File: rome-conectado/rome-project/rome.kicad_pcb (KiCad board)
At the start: 2 copper layers, 109.2 x 86.4 mm, 24 parts, among them J1 Screw_Terminal_01x02, J2 Conn_02x04_Counter_Clockwise, U3 L7805

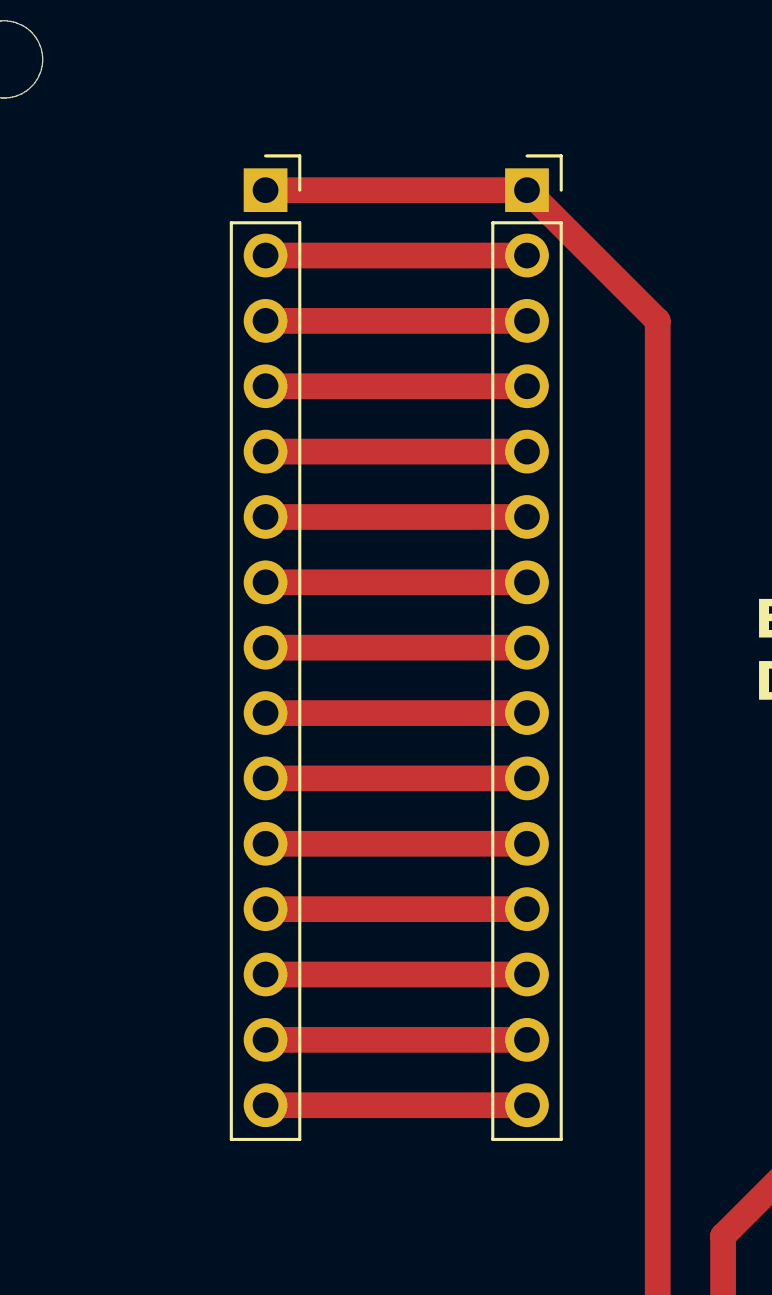
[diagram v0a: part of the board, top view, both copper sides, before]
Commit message: Update board after position adjustments
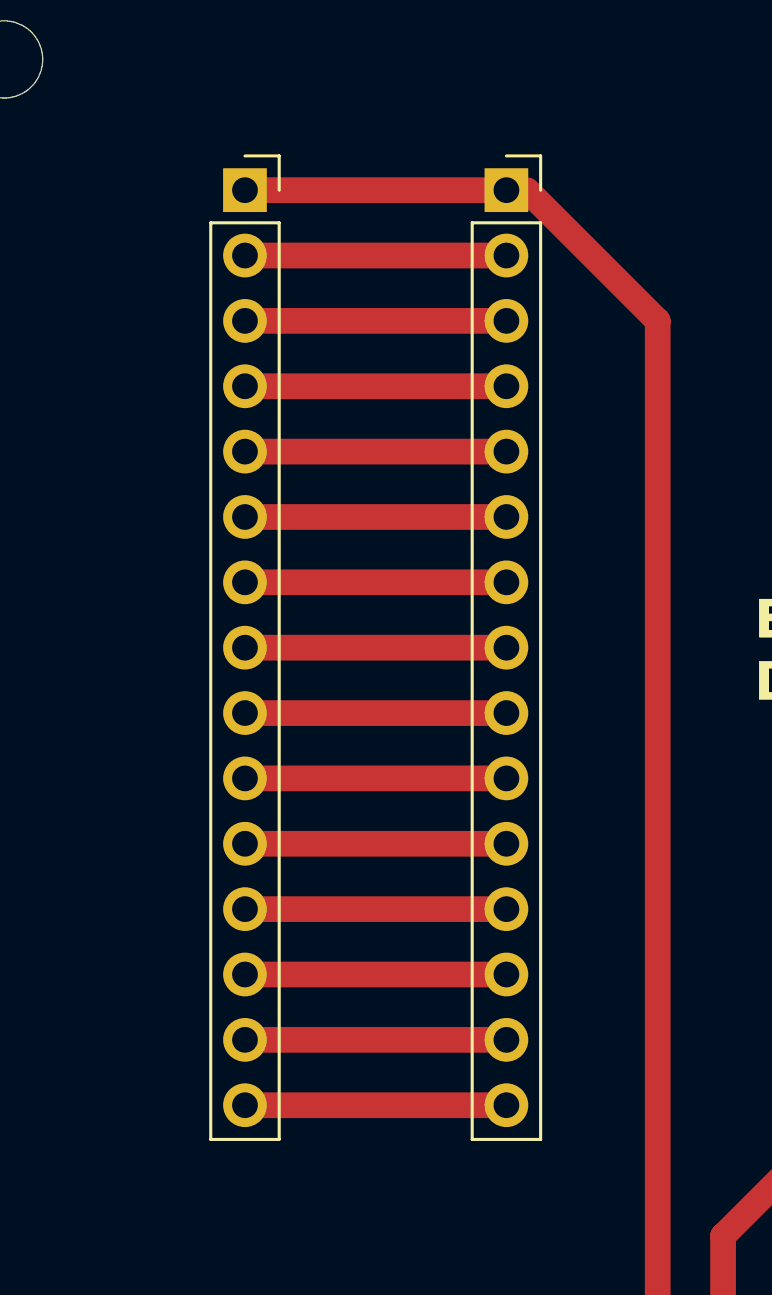
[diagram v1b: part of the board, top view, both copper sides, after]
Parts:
- moved DEV2 0.80 mm to (113.5, 73.7)
- moved DEVE2 0.80 mm to (103.3, 73.7)
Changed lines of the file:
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@@
 	(footprint "Connector_PinSocket_2.54mm:PinSocket_1x15_P2.54mm_Vertical"
 		(layer "F.Cu")
-		(at 114.3 73.66)
+		(at 113.5 73.66)
 		(descr "Through hole straight socket strip, 1x15, 2.54mm pitch, single row (from Kicad 4.0.7), script generated")
 		(tags "Through hole socket strip THT 1x15 2.54mm single row")
@@
 	(footprint "Connector_PinSocket_2.54mm:PinSocket_1x15_P2.54mm_Vertical"
 		(layer "F.Cu")
-		(at 104.14 73.66)
+		(at 103.34 73.66)
 		(descr "Through hole straight socket strip, 1x15, 2.54mm pitch, single row (from Kicad 4.0.7), script generated")
 		(tags "Through hole socket strip THT 1x15 2.54mm single row")
@@
 	)
 	(gr_text_box "3v3\nGND\nD15\nD2\nD4\nRX2\nTX2\nD5\nD18\nD19\nD21\nRX0\nTX0\nD22\nD23"
-		(start 97.624013 71.521471)
-		(end 102.704013 89.301471)
+		(start 96.824013 71.521471)
+		(end 101.904013 89.301471)
 		(margins 1.0025 1.0025 1.0025 1.0025)
 		(layer "F.SilkS")
@@
 	)
 	(segment
-		(start 114.3 76.2)
-		(end 104.14 76.2)
+		(start 113.5 76.2)
+		(end 103.34 76.2)
 		(width 1)
 		(layer "F.Cu")
@@
 	)
 	(segment
-		(start 114.3 81.28)
-		(end 104.14 81.28)
+		(start 113.5 81.28)
+		(end 103.34 81.28)
 		(width 1)
 		(layer "F.Cu")
@@
 	)
 	(segment
-		(start 114.3 86.36)
-		(end 104.14 86.36)
+		(start 113.5 86.36)
+		(end 103.34 86.36)
 		(width 1)
 		(layer "F.Cu")
@@
 	)
 	(segment
-		(start 114.3 96.52)
-		(end 104.14 96.52)
+		(start 113.5 96.52)
+		(end 103.34 96.52)
 		(width 1)
 		(layer "F.Cu")
@@
 	)
 	(segment
-		(start 114.3 99.06)
-		(end 104.14 99.06)
+		(start 113.5 99.06)
+		(end 103.34 99.06)
 		(width 1)
 		(layer "F.Cu")
@@
 	)
 	(segment
-		(start 114.3 106.68)
-		(end 104.14 106.68)
+		(start 113.5 106.68)
+		(end 103.34 106.68)
 		(width 1)
 		(layer "F.Cu")
@@
 	)
 	(segment
-		(start 114.3 83.82)
-		(end 104.14 83.82)
+		(start 113.5 83.82)
+		(end 103.34 83.82)
 		(width 1)
 		(layer "F.Cu")
@@
 	)
 	(segment
-		(start 114.3 101.6)
-		(end 104.14 101.6)
+		(start 113.5 101.6)
+		(end 103.34 101.6)
 		(width 1)
 		(layer "F.Cu")
@@
 	)
 	(segment
-		(start 114.3 93.98)
-		(end 104.14 93.98)
+		(start 113.5 93.98)
+		(end 103.34 93.98)
 		(width 1)
 		(layer "F.Cu")
@@
 	)
 	(segment
-		(start 114.3 104.14)
-		(end 104.14 104.14)
+		(start 113.5 104.14)
+		(end 103.34 104.14)
 		(width 1)
 		(layer "F.Cu")
@@
 	)
 	(segment
-		(start 114.3 78.74)
-		(end 104.14 78.74)
+		(start 113.5 78.74)
+		(end 103.34 78.74)
 		(width 1)
 		(layer "F.Cu")
@@
 	)
 	(segment
-		(start 114.3 88.9)
-		(end 104.14 88.9)
+		(start 113.5 88.9)
+		(end 103.34 88.9)
 		(width 1)
 		(layer "F.Cu")
@@
 	)
 	(segment
-		(start 114.3 91.44)
-		(end 104.14 91.44)
+		(start 113.5 91.44)
+		(end 103.34 91.44)
 		(width 1)
 		(layer "F.Cu")
@@
 	)
 	(segment
-		(start 114.3 73.66)
-		(end 104.14 73.66)
+		(start 113.5 73.66)
+		(end 103.34 73.66)
 		(width 1)
 		(layer "F.Cu")
@@
 	)
 	(segment
-		(start 114.3 109.22)
-		(end 104.14 109.22)
-		(width 1)
-		(layer "F.Cu")
+		(start 113.5 109.22)
+		(end 103.34 109.22)
+		(width 1)
+		(layer "F.Cu")

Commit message: Update project and WRE2026 paper
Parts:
- removed UNK_HOLE_1 (x4): , dummyfp1
- moved svg2mod 35.9 mm to (156.7, 80.6)
- moved J2 14.2 mm to (180.3, 87.6)
- moved HBE1 13.0 mm to (161.3, 118.1)
- moved U3 12.7 mm to (185.4, 76.2)
- moved D3 11.9 mm to (194.8, 76.2)
- moved J1 11.9 mm to (194.8, 101.6)
- moved HBIN1 8.94 mm to (171.4, 122.3)
- moved HBOUT1 8.94 mm to (185.2, 122.3)
- moved HBP1 8.94 mm to (168.4, 114.3)
- moved HBIN2 8.94 mm to (171.4, 128.3)
- moved HBOUT2 8.94 mm to (185.2, 128.3)
- moved LVE1 8.03 mm to (106.7, 116.8)
- moved HVE1 8.03 mm to (132.1, 116.8)
- moved HV1 7.62 mm to (124.3, 116.8)
- moved LV1 7.62 mm to (114.3, 116.8)
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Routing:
- net GND: track 174.6 -> 255.6 mm
- net +3.3V: track 80.4 -> 69.2 mm
- net VIN: track 13.8 -> 7.97 mm
- net OUTA2: track 12.0 -> 6.90 mm
- net IN2: track 15.6 -> 10.5 mm
- net OUTB2: track 11.6 -> 6.52 mm
- net OUTB1: track 11.6 -> 6.52 mm
- net IN4: track 15.2 -> 10.2 mm
- net IN3: track 15.2 -> 10.2 mm
- net OUTA1: track 12.0 -> 6.90 mm
- net IN1: track 15.6 -> 10.5 mm
- net TX2: track 10.2 -> 6.82 mm
- net TX0: track 10.2 -> 6.82 mm
- net RX2: track 10.2 -> 6.82 mm
- net RX0: track 10.2 -> 6.82 mm
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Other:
- board size 109.2 x 86.4 mm -> 103 x 67 mm
- board text removed: "9~12V"
